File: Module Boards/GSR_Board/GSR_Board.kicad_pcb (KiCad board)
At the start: 4 copper layers, 23.4 x 10.7 mm, 58 parts, among them U1 AD8236ARMZ-R7, U2 LTC2064IDD#PBF, U3 MAX5419LETA+T, U4 MAX5419LETA+T, U5 TPS7A9401DSCR, U6 TXS0102DQER

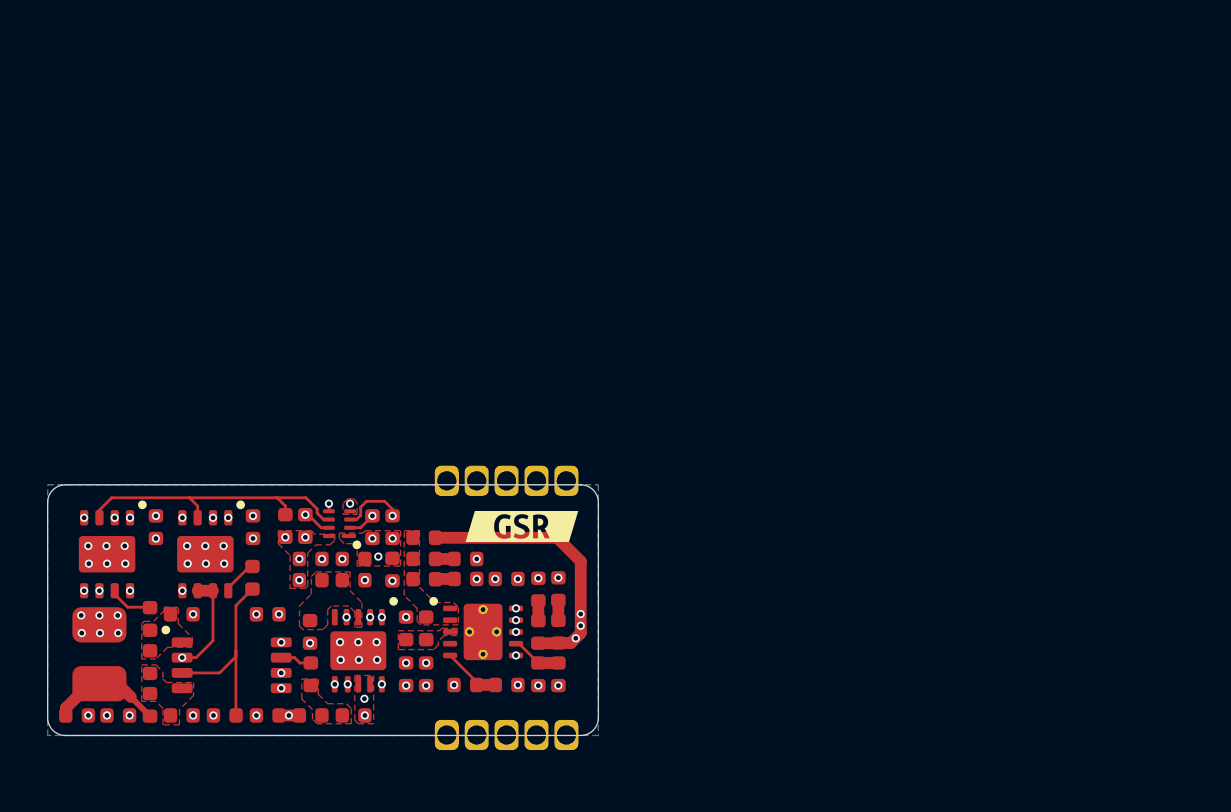
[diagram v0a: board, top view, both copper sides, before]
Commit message: Added ADC to board and partially placed/routed the updated board
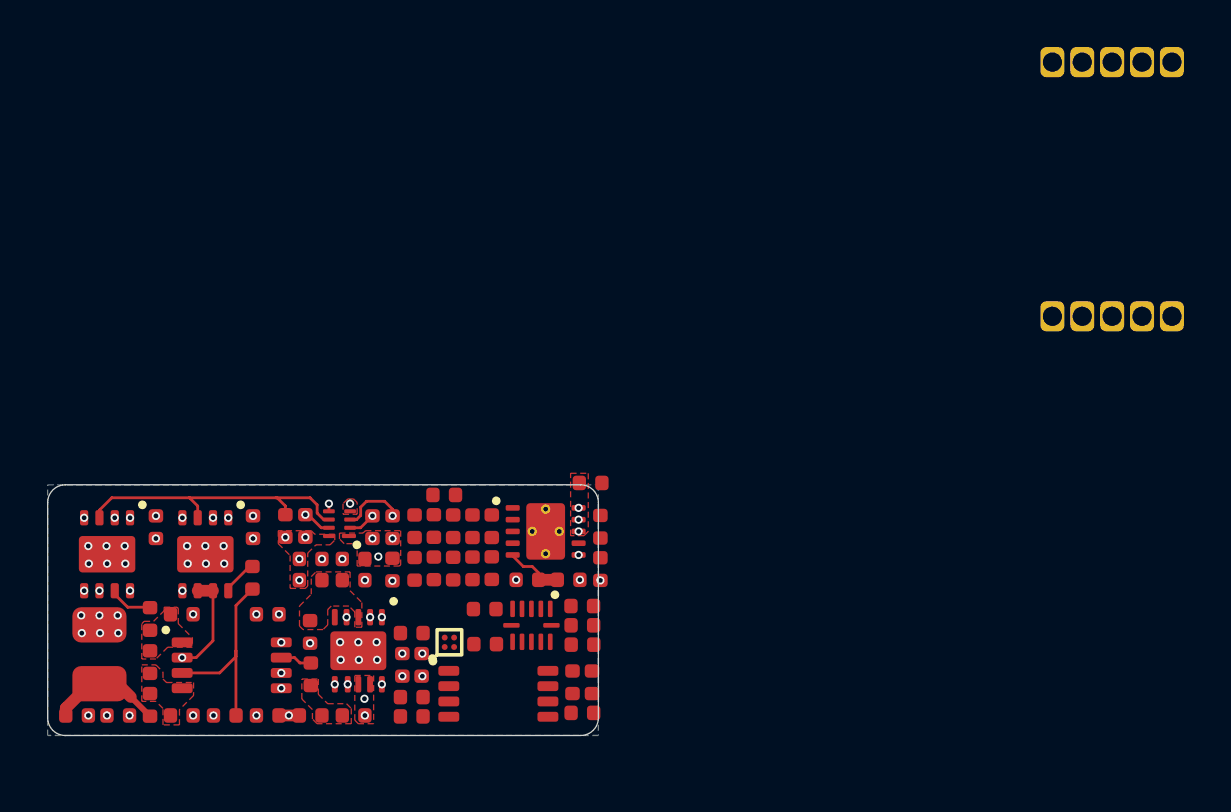
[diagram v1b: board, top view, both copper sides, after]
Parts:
- removed kibuzzard-66FA4E9D: G***, kibuzzard-66FA4E9D
- added C16: 10u0 16V, X-MODs_PcbLib:C0402, F.Cu at (138.1, 97.2)
- added C22: 100n 10V, X-MODs_PcbLib:C0402, F.Cu at (138.9, 97.2)
- added C23: 100n 10V, X-MODs_PcbLib:C0402, F.Cu at (138.5, 94.0)
- added C24: 100n 10V, X-MODs_PcbLib:C0402, F.Cu at (138.5, 95.6)
- added C25: 1u00 10V, X-MODs_PcbLib:C0402, F.Cu at (131.2, 95.1)
- added R20: 1M00, X-MODs_PcbLib:R0402, F.Cu at (138.5, 94.8)
- added R23: 0R00, X-MODs_PcbLib:R0402, F.Cu at (131.2, 98.6)
- added R26: 0R00, X-MODs_PcbLib:R0402, F.Cu at (131.2, 97.8)
- added R27: 22R0, X-MODs_PcbLib:R0402, F.Cu at (138.5, 98.5)
- added R28: 56K0, X-MODs_PcbLib:R0402, F.Cu at (134.3, 94.1)
- added R29: 56K0, X-MODs_PcbLib:R0402, F.Cu at (134.3, 95.6)
- added U7: LTC1864LIMS8#PBF, X-MODs_PcbLib:MSOP-8, F.Cu at (134.9, 97.7)
- added U8: TXB0104RUTR, X-MODs_PcbLib:UQFN-12_1.7x2mm, F.Cu at (136.3, 94.8)
- added U9: TPS22916CYFPR, X-MODs_PcbLib:DSBGA-4_0.74x0.74mm, F.Cu at (132.8, 95.5)
- moved J2 31.3 mm to (153.2, 76.3)
- moved C21 7.58 mm to (131.3, 90.6), turned to -90 degrees
- moved C15 6.52 mm to (139.2, 90.6), turned to 90 degrees
- moved C20 6.32 mm to (132.2, 90.5), turned to -90 degrees
- moved R24 6.17 mm to (131.3, 92.4), turned to -90 degrees
- moved C17 5.42 mm to (138.8, 88.7), turned to 0 degrees
- moved R15 5.19 mm to (139.2, 92.4)
- moved R18 5.19 mm to (136.1, 92.8)
- moved R19 5.19 mm to (137.9, 92.8)
- moved R16 5.16 mm to (134.6, 90.6)
- moved U5 5.03 mm to (136.9, 90.8)
- moved R25 4.53 mm to (132.2, 92.3), turned to -90 degrees
- moved R17 4.45 mm to (134.6, 92.3), turned to -90 degrees
- moved C18 3.04 mm to (133.8, 90.6), turned to -90 degrees
- moved FB1 2.01 mm to (132.6, 89.2), turned to 180 degrees
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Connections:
- net /[2] GSR/V_IA_OUT renamed V_IA_OUT
- R5 pad 1: +1V8 -> LVL_SHIFTER_EN
- R5 pad 2: LVL_SHIFTER_EN -> GND
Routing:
- net +3V3: track 17.0 -> 0.00 mm, vias 3 -> 0
- net +1V8: track 12.1 -> 2.19 mm
- net /[1] Power Regulation & Level Shifting/NR/SS: track 2.14 -> 0.13 mm
- net Net-(C21-Pad2): track 0.85 -> 0.00 mm
- net Net-(C20-Pad2): track 0.84 -> 0.00 mm
- net Net-(C19-Pad2): track 0.79 -> 0.00 mm
- net Net-(C18-Pad2): track 0.79 -> 0.01 mm
- net LVL_SHIFTER_EN: track 16.4 -> 17.0 mm
- net GND: vias 54 -> 47
- net +3VA: vias 23 -> 22
- removed copper zone on F.Cu, net /[1] Power Regulation & Level Shifting/+3V3_FILT
- removed copper zone on F.Cu, net /[1] Power Regulation & Level Shifting/EN_UV

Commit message: Finished Routing of GSR Board
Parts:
- U5: footprint X-MODs_PcbLib:WSON-8-3.15x3.15mm -> X-MODs_PcbLib:WSON-10-3.15x3.15mm
- moved J2 30.8 mm to (127.9, 94.0)
- moved C25 7.80 mm to (138.9, 94.0)
- moved U9 6.02 mm to (138.8, 95.2)
- moved R5 5.00 mm to (125.4, 92.5)
- moved R18 4.45 mm to (138.8, 89.3)
- moved R19 4.44 mm to (135.2, 89.3), turned to 180 degrees
- moved C17 1.90 mm to (137.0, 89.3), turned to 180 degrees
- moved C23 1.26 mm to (137.2, 94.0)
- moved C24 1.26 mm to (137.2, 95.6)
- moved R20 1.26 mm to (137.2, 94.8)
- moved R29 1.26 mm to (133.1, 95.6)
- moved U8 1.26 mm to (135.1, 94.8)
- moved R28 1.25 mm to (133.1, 94.0)
- moved U5 0.72 mm to (137.0, 91.5)
- moved C22 0.46 mm to (139.3, 97.2)
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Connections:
- J2 pad 1: GSR -> GND
- J2 pad 10: SCL_1V8 -> +1V8
- J2 pad 2: GND -> LVL_SHIFTER_EN
- J2 pad 3: +1V8 -> GND
- J2 pad 4: GND -> ADC_EN
- J2 pad 5: +3V3 -> GND
- J2 pad 6: LVL_SHIFTER_EN -> V_IA_OUT
- J2 pad 8: SDA_1V8 -> GSR
- J2 pad 9: GND -> +3V3
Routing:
- net ADC_EN: track 0.00 -> 24.8 mm, vias 0 -> 2
- net SPI_CS_1V8: track 0.00 -> 21.2 mm, vias 0 -> 1
- net SPI_SCK_1V8: track 0.00 -> 19.7 mm, vias 0 -> 1
- net SPI_MISO_1V8: track 0.00 -> 19.3 mm, vias 0 -> 1
- net +1V8: track 2.19 -> 15.5 mm, vias 3 -> 5
- net LVL_SHIFTER_EN: track 17.0 -> 28.6 mm
- net V_IA_OUT: track 1.35 -> 11.9 mm, vias 0 -> 2
- net SPI_CS_3V: track 0.00 -> 7.48 mm, vias 0 -> 2
- net SPI_MISO_3V: track 0.00 -> 6.99 mm, vias 0 -> 2
- net +3V3: track 0.00 -> 4.79 mm, vias 0 -> 4
- net Net-(U5-FB_PG): track 2.53 -> 7.29 mm, vias 0 -> 3
- net +3VA_ADC: track 0.00 -> 4.26 mm
- net SPI_SCK_3V: track 0.00 -> 4.07 mm, vias 0 -> 2
- net SCL_1V8: track 5.48 -> 8.89 mm
- net +3VA: track 0.00 -> 2.50 mm, vias 22 -> 20
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- added copper zone on In2.Cu, net +1V8
- added copper zone on F.Cu, net +3V3
- added copper zone on In2.Cu, net +3V3
- added copper zone on In3.Cu, net +3VA
- added copper zone on F.Cu, net +3VA_ADC
- added copper zone on F.Cu, net /[1] Power Regulation & Level Shifting/+3V3_FILT
- added copper zone on B.Cu, net GND
- removed copper zone on B.Cu, net +3VA
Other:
- board size 23.4 x 10.7 mm -> 23.9 x 11.9 mm
- copper layers 4 -> 6
